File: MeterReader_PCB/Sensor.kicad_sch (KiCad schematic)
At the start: 5 parts, among them Q1 Q_NMOS_GSD, U1 QRE1113GR

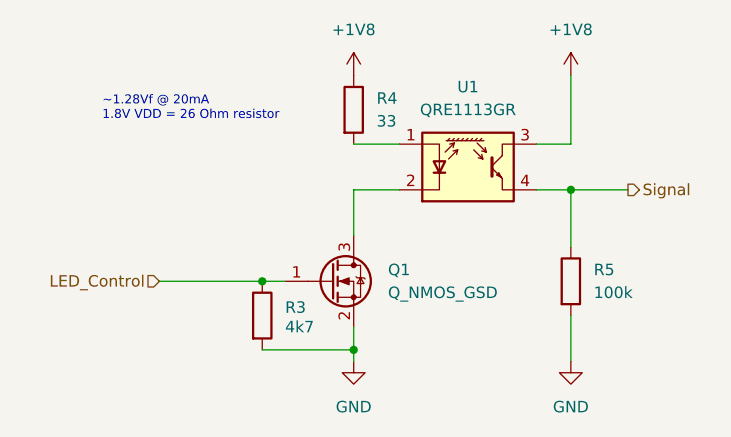
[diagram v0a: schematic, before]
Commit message: move active components onto sensor PCB, finish layout of sensor PCB
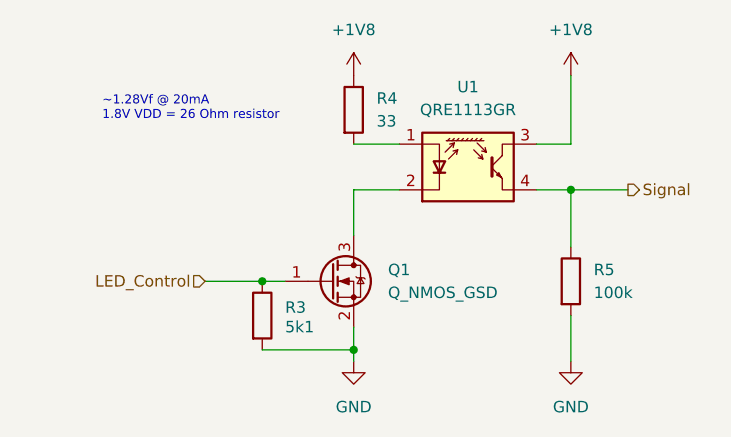
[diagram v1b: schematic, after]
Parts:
- Q1: footprint (none) -> Package_TO_SOT_SMD:SOT-23
- R3: value 4k7 -> 5k1; footprint (none) -> Resistor_SMD:R_0603_1608Metric
- R4, R5: footprint (none) -> Resistor_SMD:R_0603_1608Metric
